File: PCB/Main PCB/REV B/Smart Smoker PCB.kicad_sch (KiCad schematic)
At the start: 69 parts, among them J1 393570002, J2 1051330001, J4 Hopper, J5 Lid, Q1 25V 1.5A Trans, Q2 25V 1.5A Trans, U1 ESP32-WROOM-32UE_16MB, U2 DG409LEDY-T1-GE3, U3 MAX31855KASA, U4 CP2102N-Axx-xQFN20

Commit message: PCB schematic updates, Change to smaller thermocouple mux
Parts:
- removed U2: DG409LEDY-T1-GE3, SOIC16_NARROW_VIS, symbol dg409:DG409LEDY-T1-GE3
- added C?: 0.1uF 50V X7R 0603, Capacitor_SMD:C_0603_1608Metric, symbol Device:C
- added R?: 10K 1% 0603, Resistor_SMD:R_0603_1608Metric, symbol Device:R_US
- added U3: TS5A23159DGS, Package_SO:VSSOP-10_3x3mm_P0.5mm, symbol Analog_Switch:TS5A23159DGS
- gave numbers to parts that had none: 4
- renumbered H2 to H1, H3 to H2, H4 to H3, H5 to H4, R17 to R16, R16 to R17, R7 to R6, R6 to R7, TP9 to TP7, TP7 to TP8, TP8 to TP9, U3 to U4, U4 to U5
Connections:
- net +3.3V: now also C?.2, U3.8 (VCC)
- net GND: now also C?.1, R?.2, U3.3 (GND)
- net IO2: now also R?.1, U3.1, U3.5
- net MUX_OUT_+: now also U3.10
- net MUX_OUT_-: now also U3.6
- net Probe1+: now also U3.9
- net Probe1-: now also U3.7
- net Probe2+: now also U3.2
- net Probe2-: now also U3.4
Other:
- note removed: "Smaller Mux?"
- moved on the sheet: AE1, C1, C2, C3, C4, C7, C8, C9, D5, H1, H2, H3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

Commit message: PCB schematic updates, Reboot circuit fixed
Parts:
- removed C5: 0.1uF 50V X7R 0603, Capacitor_SMD:C_0603_1608Metric, symbol Device:C
- removed R3: 10K 1% 0603, Resistor_SMD:R_0603_1608Metric, symbol Device:R_US
- added C?: 0.1uF 50V X7R 0603, Capacitor_SMD:C_0603_1608Metric, symbol Device:C
- added R?: 10K 1% 0603, Resistor_SMD:R_0603_1608Metric, symbol Device:R_US
- added U?: STM811SW16F, Customs Smoker:STM811SW16F, symbol STM811SW16F:STM811SW16F
- gave numbers to parts that had none: 2
- renumbered C9 to C10, C10 to C11, C11 to C12, C3 to C4, C4 to C5, C6 to C7, C7 to C8, C8 to C9, R9 to R10, R10 to R11, R11 to R12, R12 to R13, R13 to R14, R14 to R15, R15 to R16, R16 to R17, R17 to R18, R18 to R19, R19 to R20, R20 to R21, R21 to R22, R4 to R5, R5 to R6, R6 to R7, R7 to R8, R8 to R9, U3 to U2, U4 to U3, U5 to U4
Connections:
- net +3.3V: now also C?.2, R?.2, U?.4 (VCC)
- net EN: now also R?.1, U?.2 (*RST); no longer S1.2
- net GND: now also S1.2, C?.1, U?.1 (VSS); no longer S1.1
- new net: S1.1, U?.3 (*MR)
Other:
- note added: "Is this needed?"
- note removed: "Look into auto reboot circuit"
- moved on the sheet: AE1, C1, C10, C11, C12, C2, C3, C4, C5, C7, C8, C9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

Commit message: PCB schematic updates, Changed transistor on reboot to double
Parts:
- removed Q1, Q2: 25V 1.5A Trans, Package_TO_SOT_SMD:SOT-23-3, symbol Transistor_BJT:S8050
- added Q? (x2): MBT3904DW1, Package_TO_SOT_SMD:SOT-363_SC-70-6, symbol Transistor_BJT:MBT3904DW1
- gave numbers to parts that had none: 3
- renumbered C12 to C10, C7 to C12, C8 to C6, C9 to C7, C10 to C8, C11 to C9, J3 to J2, J4 to J3, J5 to J4, J6 to J5, J7 to J6, J8 to J7, J2 to J8, R6 to R10, R8 to R11, R9 to R12, R11 to R13, R15 to R14, R16 to R15, R17 to R16, R18 to R17, R19 to R18, R20 to R19, R5 to R4, R7 to R5, R10 to R6, R12 to R7, R13 to R8, R14 to R9, S2 to S1, S1 to S2, TP7 to TP1, TP1 to TP2, TP2 to TP3, TP3 to TP4, TP4 to TP5, TP5 to TP6, TP6 to TP7
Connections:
- net DTR: now also Q?.4 (E2)
- net EN: now also Q?.6 (C1)
- net IO0: now also Q?.3 (C2)
- net RTS: now also Q?.1 (E1)
- net at R10.2: now also Q?.2 (B1)
- net at R12.2: now also Q?.5 (B2)
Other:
- moved on the sheet: C6, C7, C8, D5, J8, R10, R11, R12, R13, R14, R15, R16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

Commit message: PCB schematic updates, Cleanup and Add LEDS
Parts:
- added C? (x4): 0.1uF 50V X7R 0603, Capacitor_SMD:C_0603_1608Metric, symbol Device:C
- added C?: 1uF 16V X7R 0603, Capacitor_SMD:C_0603_1608Metric, symbol Device:C
- added C? (x5): 10uF 16V X5R 0805, Capacitor_SMD:C_0805_2012Metric, symbol Device:C
- added D?: Y/G 2.2V 20mA, LED_SMD:LED_0603_1608Metric, symbol Device:LED
- added D?: Y 2V 20mA, LED_SMD:LED_0603_1608Metric, symbol Device:LED
- added PS?: IRM-05-5, Converter_ACDC:Converter_ACDC_MeanWell_IRM-05-xx_THT, symbol Converter_ACDC:IRM-05-5
- added PS?: IRM-10-3.3, Converter_ACDC:Converter_ACDC_MeanWell_IRM-10-xx_THT, symbol Converter_ACDC:IRM-10-3.3
- added R?: 50Ohm 0.1% 0603, Resistor_SMD:R_0603_1608Metric, symbol Device:R_US
- added R?: 250Ohm 0.1% 0603, Resistor_SMD:R_0603_1608Metric, symbol Device:R_US
- added R?: 470Ohm 1% 0603, Resistor_SMD:R_0603_1608Metric, symbol Device:R_US
- added R?: 140Ohm 1% 0603, Resistor_SMD:R_0603_1608Metric, symbol Device:R_US
- added U?: TPS2115APWR, Customs Smoker:PW8-M, symbol TPS2115APWR:TPS2115APWR
- added U?: AMS1117-3.3, Package_TO_SOT_SMD:TO-252-2, symbol Regulator_Linear:AMS1117-3.3
- U4: value CP2102N-Axx-xQFN20 -> CP2102N-A02-GQFN24
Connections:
- net +3.3V: now also C?.1, R?.1, R?.2, U?.7 (OUT); no longer R4.1, R6.1
- net +3.3VA: now also R6.1, C?.1, C?.2, C?.2, PS?.4 (+Vo), U?.6 (1N2)
- net +3.3VP: now also R4.1, C?.1, C?.1, C?.2, U?.2 (VO), U?.8 (1N1)
- net +5V: now also C?.1, C?.2, PS?.4 (+Vo), R?.1; no longer R5.1
- net +5VA: now also R5.1, C?.1, U?.3 (VI)
- net AC_L: now also PS?.2 (AC/L), PS?.2 (AC/L)
- net AC_N: now also PS?.1 (AC/N), PS?.1 (AC/N)
- net GND: now also C?.1, C?.1, C?.1, C?.1, C?.2, C?.2, C?.2, C?.2, C?.2, C?.2, D?.1 (K), PS?.3 (-Vo), PS?.3 (-Vo), R?.1, R?.2, U?.1 (GND), U?.3 (D1), U?.5 (GND)
- net IO17: now also D?.1 (K)
- net IO_4 renamed IO4
- new net: D?.2 (A), R?.2 (x2)
- new net: R?.1, U?.4 (ILIM)
- no-connect marks 17 -> 19
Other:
- removed sheet Power
- note added: "2A Limit"
- note added: "3.3V Redundancy"
- note added: "AC-DC MAIN"
- note added: "AC-DC Power"
- note added: "AC-DC USB"
- note added: "Adjust Colors"
- note added: "USB Power"
- moved on the sheet: C1, C2, D1, D2, D3, J1, J2, J3, J4, J5, J6, J7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

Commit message: PCB schematic updates, Fix LED part number and clean up schematic. Added test points
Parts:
- removed D4: ASMB-KTF0-0A306, Customs Smoker:LED_ASMB-KTF0-0A306, symbol ASMB-KTF0-0A306:ASMB-KTF0-0A306
- removed D?: Y/G 2.2V 20mA, LED_SMD:LED_0603_1608Metric, symbol Device:LED
- removed D?: Y 2V 20mA, LED_SMD:LED_0603_1608Metric, symbol Device:LED
- removed R4: 470Ohm 1% 0603, Resistor_SMD:R_0603_1608Metric, symbol Device:R_US
- removed R5: 140Ohm 1% 0603, Resistor_SMD:R_0603_1608Metric, symbol Device:R_US
- removed R7, R8: 20Ohm 1% 0603, Resistor_SMD:R_0603_1608Metric, symbol Device:R_US
- removed R9: 64.9Ohm 1% 0603, Resistor_SMD:R_0603_1608Metric, symbol Device:R_US
- added C18, C22, C23: 0.1uF 50V X7R 0603, Capacitor_SMD:C_0603_1608Metric, symbol Device:C
- added D10, D12, D7: Schottky 30v 200mA, Customs Smoker:RB521S30T1G-M, symbol Diode:1N6857UR
- added D11, D6, D9: B 3.2 20mA 0603, LED_SMD:LED_0603_1608Metric, symbol Device:LED
- added D4, D5: R 2.0V 20mA, LED_SMD:LED_0603_1608Metric, symbol Device:LED
- added JP1, JP2, JP3, JP4, JP5, JP6: SolderJumper_3_Open, symbol Jumper:SolderJumper_3_Open
- added Q1, Q2, Q4: 2N7002, Package_TO_SOT_SMD:SOT-23, symbol Transistor_FET:2N7002
- added R12, R25, R32: 91Ohm 1% 0603, Resistor_SMD:R_0603_1608Metric, symbol Device:R_US
- added R14, R22, R27: 140Ohm 1% 0603, Resistor_SMD:R_0603_1608Metric, symbol Device:R_US
- added R16, R26, R36: 0 Ohm 0603, Resistor_SMD:R_0603_1608Metric, symbol Device:R_US
- added R2: 64.9Ohm 1% 0603, Resistor_SMD:R_0603_1608Metric, symbol Device:R_US
- added R28, R29, R34, R35, R37, R38: 10K 1% 0603, Resistor_SMD:R_0603_1608Metric, symbol Device:R_US
- added R3: 150Ohm 1% 0603, Resistor_SMD:R_0603_1608Metric, symbol Device:R_US
- added TP1, TP10, TP11, TP12, TP13, TP14, TP15, TP16, TP17, TP18, TP19, TP20, TP21, TP22, TP23, TP24, TP25, TP26, TP27, TP28, TP29, TP30, TP9: TP, TestPoint:TestPoint_Pad_D1.0mm, symbol Connector:TestPoint
- added U10, U12, U7: ALDP105W, Customs Smoker:PAN_ALD_PAN, symbol ALDP105W:ALDP105W
- added U11, U6, U9: TLP2362TPR_E, Customs Smoker:TLP2362, symbol TLP2362:TLP2362TPR_E
- D1: value Y 2V 20mA -> R 2.0V 20mA; Manufacturer Würth Elektronik -> ams-OSRAM USA INC.; Manufacturer Part Number 150060YS75000 -> LO Q976-PS-25-0-20-R18; Vendor Part Number 732-4981-1-ND -> 475-LOQ976-PS-25-0-20-R18CT-ND
- D2: value Y/G 2.2V 20mA -> R 2.0V 20mA; Manufacturer American Bright Optoelectronics Corporation -> ams-OSRAM USA INC.; Manufacturer Part Number BL-HGE36D-AV-TRB -> LO Q976-PS-25-0-20-R18; Vendor Part Number BL-HGE36D-AV-TRBCT-ND -> 475-LOQ976-PS-25-0-20-R18CT-ND
- D3: value R 1.8V 2mA 0603 -> R 2.0V 20mA; Manufacturer Rohm Semiconductor -> ams-OSRAM USA INC.; Manufacturer Part Number CSL1901UW1 -> LO Q976-PS-25-0-20-R18; Vendor Part Number 846-CSL1901UW1CT-ND -> 475-LOQ976-PS-25-0-20-R18CT-ND
- R6: value 750Ohm 1% 0603 -> 64.9Ohm 1% 0603; Manufacturer Part Number RC0603FR-07750RL -> RC0603FR-0764R9L; Vendor Part Number 311-750HRCT-ND -> 311-64.9HRCT-ND
- R7: renamed from R?; value 140Ohm 1% 0603 -> 150Ohm 1% 0603; Manufacturer Part Number RC0603FR-07140RL -> RC0603FR-07150RL; Vendor Part Number 311-140HRCT-ND -> 311-150HRCT-ND
- R8: renamed from R?; value 470Ohm 1% 0603 -> 64.9Ohm 1% 0603; Manufacturer Part Number RC0603FR-13470RL -> RC0603FR-0764R9L; Vendor Part Number 13-RC0603FR-13470RLCT-ND -> 311-64.9HRCT-ND
- TP2, TP5, TP6: value 3V3 TP -> TP; footprint TestPoint:TestPoint_THTPad_D1.0mm_Drill0.5mm -> TestPoint:TestPoint_Pad_D1.0mm
- TP3: value GND TP -> TP; footprint TestPoint:TestPoint_THTPad_D1.0mm_Drill0.5mm -> TestPoint:TestPoint_Pad_D1.0mm
- TP31: renamed from TP9; footprint Connector_PinHeader_2.54mm:PinHeader_1x04_P2.54mm_Vertical -> Connector_PinHeader_2.54mm:PinHeader_1x06_P2.54mm_Vertical; symbol Connector_Generic:Conn_01x04 -> Connector_Generic:Conn_01x06
- TP4: value GND TP PIN -> TP; footprint Connector_PinHeader_2.54mm:PinHeader_1x01_P2.54mm_Vertical -> TestPoint:TestPoint_Pad_D1.0mm
- TP7: value SCL TP -> TP; footprint TestPoint:TestPoint_THTPad_D1.0mm_Drill0.5mm -> TestPoint:TestPoint_Pad_D1.0mm
- TP8: value SDA TP -> TP; footprint TestPoint:TestPoint_THTPad_D1.0mm_Drill0.5mm -> TestPoint:TestPoint_Pad_D1.0mm
- gave numbers to parts that had none: 17
- renumbered C4 to C11, C5 to C12, C6 to C16, C7 to C17, C8 to C19, C9 to C20, C10 to C21, C11 to C24, C12 to C25, C3 to C6, C1 to C7, C2 to C8, D5 to D8, J8 to J3, J5 to J4, J6 to J5, J7 to J6, J3 to J7, J4 to J8, R3 to R1, R17 to R13, R13 to R15, R18 to R17, R19 to R18, R21 to R19, R22 to R20, R14 to R21, R15 to R23, R16 to R24, R10 to R30, R20 to R31, R12 to R33, R1 to R4, R2 to R5, S2 to S1, S1 to S2, TP1 to TP32, U5 to U13, U1 to U3, U3 to U4, U4 to U8
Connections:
- net +3.3V: now also JP1.3 (B), JP2.3 (B), JP3.3 (B), JP4.3 (B), JP5.3 (B), JP6.3 (B), TP16.1; no longer TP2.1
- net +3.3VA: now also TP2.1; no longer TP6.1
- net +3.3VP: now also R2.1; no longer TP5.1
- net +5V: now also C1.1, C10.2, C11.2, C13.2, C14.1, C15.1, C16.1, C17.1, C19.2, C2.2, C20.2, C21.2, C24.1, C25.2, C3.2, C4.2, C5.2, C6.1, C7.1, C8.1, C9.1, D2.1 (K), D3.1 (K), D8.1 (A), J3.5 (GND), J7.2 (Pin_2), J8.2 (Pin_2), MT1.1, MT1.COM, MT1.S1 (SHIELD), MT1.S2 (SHIELD), PS1.3 (-Vo), PS2.3 (-Vo), R1.2, R10.2, R23.1, R9.1, S1.2, S2.1, TP32.3 (Pin_3), TP6.1, U1.1 (GND), U13.1 (VSS), U2.3 (GND), U3.1 (GND), U3.15 (GND), U3.38 (GND), U3.39 (GND), U3.40 (GND), U3.41 (GND), U3.42 (GND), U3.43 (GND), U3.44 (GND), U3.45 (GND), U3.46 (GND), U3.47 (GND), U4.1 (GND), U5.3 (D1), U5.5 (GND), U8.2 (GND), U8.25 (GND), C18.1, C22.1, C23.1, D10.1 (K), D12.1 (K), D4.1 (K), D7.1 (K), JP1.1 (A), JP2.1 (A), JP3.1 (A), JP4.1 (A), JP5.1 (A), JP6.1 (A), Q1.3 (D), Q2.3 (D), Q4.3 (D), R12.1, R25.1, R32.1, TP20.1, U10.1, U11.3 (CATHODE), U11.6 (VCC), U12.1, U6.3 (CATHODE), U6.6 (VCC), U7.1, U9.3 (CATHODE), U9.6 (VCC)
- net +5VA: now also R3.1
- net AC_L: now also U10.2, U12.2, U7.2
- net AUGER: now also R14.1; no longer U3.14 (IO12)
- net Auger_+: now also U7.3
- net DTR: now also TP24.1
- net EN: now also TP21.1
- net FAN: now also R22.1; no longer U3.16 (IO13)
- net Fan_+: now also U12.3
- net I2C_SCL: now also TP14.1; no longer TP7.1
- net I2C_SDA: now also TP13.1; no longer TP8.1
- net IGNITOR: now also R27.1; no longer U3.13 (IO14)
- net IO0: now also TP26.1
- net IO17: now also D5.1 (K)
- net IO2: now also TP1.1
- net IO25: now also TP31.1 (Pin_1), R38.1, TP30.1
- net IO26: now also TP31.2 (Pin_2), R35.1, TP28.1
- net IO27: now also TP31.3 (Pin_3), R29.1, TP23.1
- net IO32: now also TP18.1
- net IO33: now also TP17.1, TP19.1
- net Ignitor_+: now also U10.3
- net MUX_OUT_+: now also TP4.1
- net MUX_OUT_-: now also TP8.1
- net Probe1+: now also TP5.1
- net Probe1-: now also TP9.1
- net Probe2+: now also TP3.1
- net Probe2-: now also TP7.1
- net RTS: now also TP25.1
- net SPI_CS: now also TP12.1
- net SPI_MISO: now also TP10.1
- net SPI_MOSI: now also TP15.1
- net SPI_SCK: now also TP11.1
- net at R7.2: now also D4.2 (A)
- net at D1.2 (A): now also R2.2
- net IO14: now reaches TP31.4 (Pin_4)
- net IO14: now also U3.13 (IO14), R37.1, TP29.1
- net at D2.2 (A): now also R3.2
- net at R8.2: now also D5.2 (A)
- removed net GND: C1.1, C10.2, C11.2, C13.2, C14.1, C15.1, C16.1, C17.1, C19.2, C2.2, C20.2, C21.2, C24.1, C25.2, C3.2, C4.2, C5.2, C6.1, C7.1, C8.1, C9.1, D2.1 (K), D3.1 (K), D8.1 (A), J3.5 (GND), J7.2 (Pin_2), J8.2 (Pin_2), MT1.1, MT1.COM, MT1.S1 (SHIELD), MT1.S2 (SHIELD), PS1.3 (-Vo), PS2.3 (-Vo), R1.2, R10.2, R23.1, R9.1, S1.2, S2.1, TP3.1, TP32.3 (Pin_3), TP4.1, U1.1 (GND), U13.1 (VSS), U2.3 (GND), U3.1 (GND), U3.15 (GND), U3.38 (GND), U3.39 (GND), U3.40 (GND), U3.41 (GND), U3.42 (GND), U3.43 (GND), U3.44 (GND), U3.45 (GND), U3.46 (GND), U3.47 (GND), U4.1 (GND), U5.3 (D1), U5.5 (GND), U8.2 (GND), U8.25 (GND)
- new net: JP5.2 (C), R37.2
- new net: D7.2 (A), R16.1, U7.4
- new net: C18.2, U6.4 (GND)
- new net: D12.2 (A), R36.1, U12.4
- new net: D11.1 (K), Q4.2 (S), R36.2
- new net: R27.2, U11.1 (ANODE)
- new net: D6.1 (K), Q1.2 (S), R16.2
- new net: C22.2, U9.4 (GND)
- new net: JP2.2 (C), R29.2
- new net: R22.2, U9.1 (ANODE)
- new net: JP3.2 (C), R34.2
- new net: D11.2 (A), R32.2
- new net: JP4.2 (C), R35.2
- new net: D10.2 (A), R26.1, U10.4
- new net: R14.2, U6.1 (ANODE)
- new net: D9.1 (K), Q2.2 (S), R26.2
- new net: JP1.2 (C), R28.2
- new net: D9.2 (A), R25.2
- new net: D6.2 (A), R12.2
- new net: JP6.2 (C), R38.2
- new net: C23.2, U11.4 (GND)
- new net IO12: R34.1, TP27.1, TP31.5 (Pin_5), U3.14 (IO12)
- new net IO13: R28.1, TP22.1, TP31.6 (Pin_6), U3.16 (IO13)
- new net Opto_Auger: Q1.1 (G), U6.5 (VO)
- new net Opto_Fan: Q4.1 (G), U9.5 (VO)
- new net Opto_Ignitor: Q2.1 (G), U11.5 (VO)
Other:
- removed sheet Loads
- note added: "Is a resistor needed here?"
- note added: "LOADS"
- note added: "Peripherials"
- note added: "Pull signal high or low"
- note removed: "Additional Test Points"
- note removed: "Adjust Colors"
- note removed: "Connectors"
- note removed: "LEDs"
- moved on the sheet: AE1, C1, C10, C11, C12, C13, C14, C15, C16, C17, C19, C2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

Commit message: PCB schematic updates, Delete lid connections, add qwiic connectors
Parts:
- removed J7: Hopper, Connector_Molex:Molex_Micro-Fit_3.0_43045-0400_2x02_P3.00mm_Horizontal, symbol Connector_Generic:Conn_02x02_Top_Bottom
- removed J8: Lid, Connector_Molex:Molex_Micro-Fit_3.0_43045-0400_2x02_P3.00mm_Horizontal, symbol Connector_Generic:Conn_02x02_Top_Bottom
- added J10: Spare2, Customs Smoker:PRT-14417, symbol PRT-14417:PRT-14417
- added J4: Hopper, Customs Smoker:PRT-14417, symbol PRT-14417:PRT-14417
- added J7: Screen, Customs Smoker:PRT-14417, symbol PRT-14417:PRT-14417
- added J9: Spare1, Customs Smoker:PRT-14417, symbol PRT-14417:PRT-14417
- AE1: value Antenna -> Antenna - FOR BOM ONLY
- JP1, JP2, JP3, JP4, JP5, JP6: footprint (none) -> Jumper:SolderJumper-3_P1.3mm_Open_RoundedPad1.0x1.5mm
- TP31: renamed from TP32; value Screen I2C -> Screen I2C - FOR BOM ONLY
- renumbered J4 to J5, J5 to J6, J6 to J8, R30 to R28, R28 to R29, R29 to R30, R36 to R34, R34 to R35, R35 to R36, TP24 to TP22, TP22 to TP23, TP23 to TP24, TP31 to TP32
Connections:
- net +3.3V: now also J10.2, J4.2, J7.2, J9.2; no longer TP31.4 (Pin_4)
- net +5V: now also D1.1 (K), D5.1 (K), J10.1, J4.1, J7.1, J9.1; no longer TP31.3 (Pin_3)
- net I2C_SCL: now also J10.4, J4.4, J7.4, J9.4; no longer TP31.2 (Pin_2)
- net I2C_SDA: now also J10.3, J4.3, J7.3, J9.3; no longer TP31.1 (Pin_1)
- net IO17: no longer D1.1 (K), D5.1 (K)
- no-connect marks 19 -> 24
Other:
- note added: "QWIIC"
- note added: "Spare Pullups/Pulldowns"
- note removed: "Is this needed?"
- moved on the sheet: JP1, JP2, JP3, JP4, JP5, JP6, R29, R30, R35, R36, R37, R38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

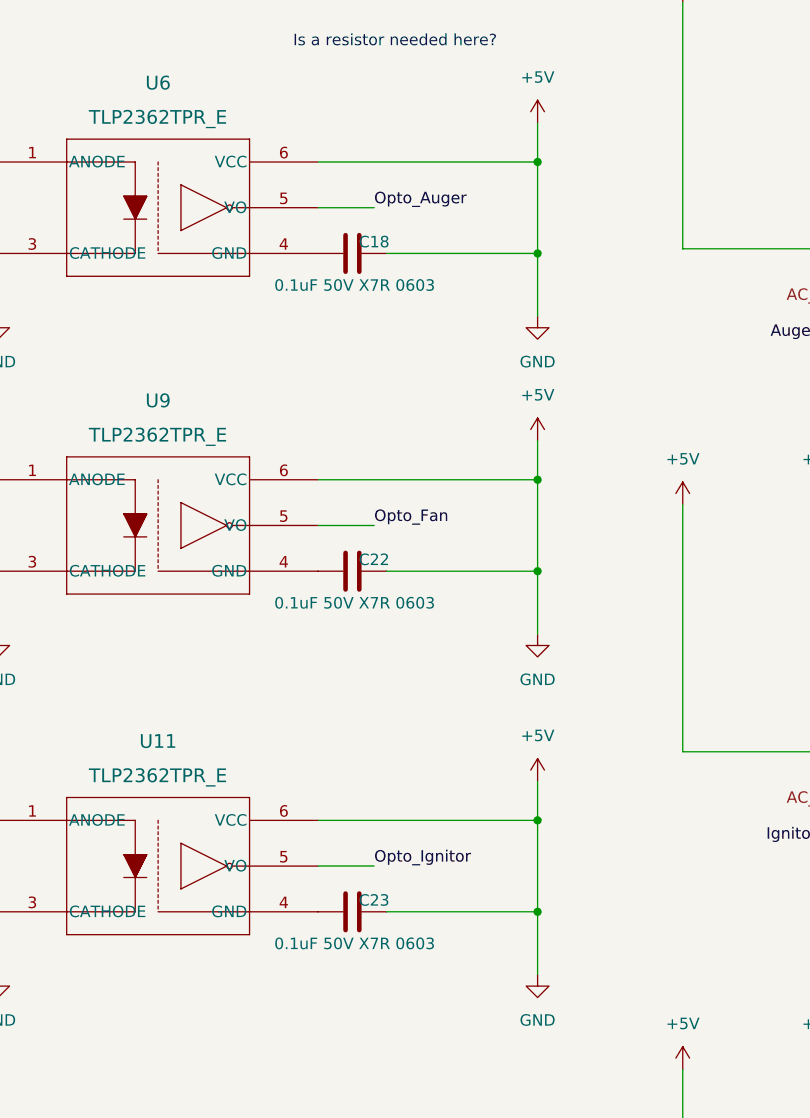
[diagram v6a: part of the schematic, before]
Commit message: PCB Layout - Begin Grouping of main PCB
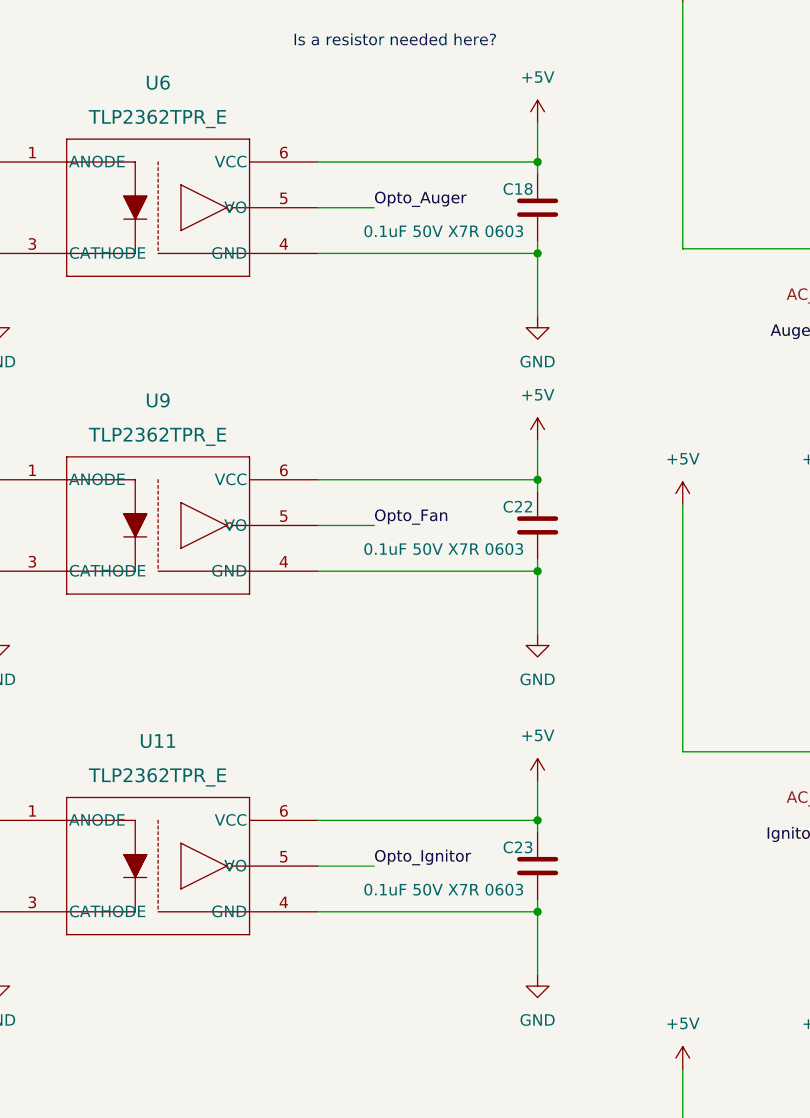
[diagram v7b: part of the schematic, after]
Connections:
- net +5V: no longer C1.1, C10.2, C11.2, C13.2, C14.1, C15.1, C16.1, C17.1, C19.2, C2.2, C20.2, C21.2, C24.1, C25.2, C3.2, C4.2, C5.2, C6.1, C7.1, C8.1, C9.1, D1.1 (K), D2.1 (K), D3.1 (K), D4.1 (K), D5.1 (K), D8.1 (A), J10.1, J3.5 (GND), J4.1, J7.1, J9.1, JP1.1 (A), JP2.1 (A), JP3.1 (A), JP4.1 (A), JP5.1 (A), JP6.1 (A), MT1.1, MT1.COM, MT1.S1 (SHIELD), MT1.S2 (SHIELD), PS1.3 (-Vo), PS2.3 (-Vo), Q1.3 (D), Q2.3 (D), Q4.3 (D), R1.2, R10.2, R23.1, R9.1, S1.2, S2.1, TP20.1, U1.1 (GND), U11.3 (CATHODE), U13.1 (VSS), U2.3 (GND), U3.1 (GND), U3.15 (GND), U3.38 (GND), U3.39 (GND), U3.40 (GND), U3.41 (GND), U3.42 (GND), U3.43 (GND), U3.44 (GND), U3.45 (GND), U3.46 (GND), U3.47 (GND), U4.1 (GND), U5.3 (D1), U5.5 (GND), U6.3 (CATHODE), U8.2 (GND), U8.25 (GND), U9.3 (CATHODE)
- net GND: now reaches C18.2, U6.4 (GND)
- net GND: now also C1.1, C10.2, C11.2, C13.2, C14.1, C15.1, C16.1, C17.1, C19.2, C2.2, C20.2, C21.2, C22.2, C23.2, C24.1, C25.2, C3.2, C4.2, C5.2, C6.1, C7.1, C8.1, C9.1, D1.1 (K), D2.1 (K), D3.1 (K), D4.1 (K), D5.1 (K), D8.1 (A), J10.1, J3.5 (GND), J4.1, J7.1, J9.1, JP1.1 (A), JP2.1 (A), JP3.1 (A), JP4.1 (A), JP5.1 (A), JP6.1 (A), MT1.1, MT1.COM, MT1.S1 (SHIELD), MT1.S2 (SHIELD), PS1.3 (-Vo), PS2.3 (-Vo), Q1.3 (D), Q2.3 (D), Q4.3 (D), R1.2, R10.2, R23.1, R9.1, S1.2, S2.1, TP20.1, U1.1 (GND), U11.3 (CATHODE), U11.4 (GND), U13.1 (VSS), U2.3 (GND), U3.1 (GND), U3.15 (GND), U3.38 (GND), U3.39 (GND), U3.40 (GND), U3.41 (GND), U3.42 (GND), U3.43 (GND), U3.44 (GND), U3.45 (GND), U3.46 (GND), U3.47 (GND), U4.1 (GND), U5.3 (D1), U5.5 (GND), U6.3 (CATHODE), U8.2 (GND), U8.25 (GND), U9.3 (CATHODE), U9.4 (GND)
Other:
- moved on the sheet: C22

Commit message: PCB Layout - Continue Grouping layout
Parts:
- added JP1, JP2, JP5: SolderJumper_3_Open, Jumper:SolderJumper-3_P1.3mm_Open_RoundedPad1.0x1.5mm, symbol Jumper:SolderJumper_3_Open
- added R13, R27, R35: 10K 1% 0603, Resistor_SMD:R_0603_1608Metric, symbol Device:R_US
- added TP? (x6): TP, TestPoint:TestPoint_Pad_D1.0mm, symbol Connector:TestPoint
- renumbered JP1 to JP3, JP2 to JP4, JP3 to JP6, JP4 to JP7, JP5 to JP8, JP6 to JP9, R13 to R14, R14 to R15, R15 to R16, R16 to R17, R17 to R18, R18 to R19, R19 to R20, R20 to R21, R21 to R22, R22 to R23, R23 to R24, R24 to R25, R25 to R26, R26 to R28, R27 to R29, R28 to R30, R29 to R31, R30 to R32, R31 to R33, R32 to R34, R33 to R36, R34 to R37, R35 to R38, R36 to R39, R37 to R40, R38 to R41
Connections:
- net IO15 is gone; now on net Auger: U3.23 (IO15)
- net IO23 is gone; now on net Ignitor: U3.37 (IO23)
- net IO4 is gone; now on net Fan: U3.26 (IO4)
- net +3.3V: now also JP1.3 (B), JP2.3 (B), JP5.3 (B)
- net GND: now also JP1.1 (A), JP2.1 (A), JP5.1 (A)
- net Opto_Auger: now also R13.2, TP?.1
- net Opto_Fan: now also R35.2, TP?.1
- net Opto_Ignitor: now also R27.2, TP?.1
- net at R29.2, U11.1 (ANODE): now also TP?.1
- net at R23.2, U9.1 (ANODE): now also TP?.1
- net at R15.2, U6.1 (ANODE): now also TP?.1
- net AUGER renamed Auger
- net FAN renamed Fan
- net IGNITOR renamed Ignitor
- new net: JP5.2 (C), R35.1
- new net: JP1.2 (C), R13.1
- new net: JP2.2 (C), R27.1
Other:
- note added: "Pull Low"
- note removed: "Pull signal high or low"
- moved on the sheet: TP16
